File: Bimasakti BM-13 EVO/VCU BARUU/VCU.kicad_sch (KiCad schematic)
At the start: 3 parts, among them U1 Teensy4.1, U2 SN65HVD230

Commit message: add footprint library to project
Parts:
- U1: footprint (none) -> teensy4.1:Teensy41
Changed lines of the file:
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@@
 			)
 		)
-		(property "Footprint" ""
+		(property "Footprint" "teensy4.1:Teensy41"
 			(at 100.33 101.6 0)
 			(effects

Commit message: test
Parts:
- added R2: R, Resistor_SMD:R_0201_0603Metric, symbol Device:R
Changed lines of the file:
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@@
+	)
+	(symbol
+		(lib_id "Device:R")
+		(at 199.39 99.06 0)
+		(unit 1)
+		(exclude_from_sim no)
+		(in_bom yes)
+		(on_board yes)
+		(dnp no)
+		(fields_autoplaced yes)
+		(property "Reference" "R2"
+			(at 201.93 97.7899 0)
+			(effects
+				(font
+					(size 1.27 1.27)
+				)
+				(justify left)
+			)
+		)
+		(property "Value" "R"
+			(at 201.93 100.3299 0)
+			(effects
+				(font
+					(size 1.27 1.27)
+				)
+				(justify left)
+			)
+		)
+		(property "Footprint" "Resistor_SMD:R_0201_0603Metric"
+			(at 197.612 99.06 90)
+			(effects
+				(font
+					(size 1.27 1.27)
+				)
+				(hide yes)
+			)
+		)
+		(property "Datasheet" "~"
+			(at 199.39 99.06 0)
+			(effects
+				(font
+					(size 1.27 1.27)
+				)
+				(hide yes)
+			)
+		)
+		(property "Description" "Resistor"
+			(at 199.39 99.06 0)
+			(effects
+				(font
+					(size 1.27 1.27)
+				)
+				(hide yes)
+			)
+		)
+		(pin "2"
+		)
+		(pin "1"
+		)
+		(instances
+			(project ""
+				(path "/94e77d80-6817-4c0b-8f3e-96c98b3294f0"
+					(reference "R2")
+					(unit 1)
+				)
+			)
+		)
 	)
 	(symbol

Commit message: test kapasitor
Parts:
- added C1, C2, C3, C4, C5: C, symbol Device:C
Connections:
- net at R2.1: now also C3.1
- net at R2.2: now also C1.2
- new net: C4.1, C5.1
- new net: C2.1, C4.2
- new net: C1.1, C2.2

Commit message: Revert "add footprint library to project"
This reverts commit c2ea81f1652adadaa2769e08c07f448226fedb71.
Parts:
- U1: footprint teensy4.1:Teensy41 -> (none)
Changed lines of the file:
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@@
 			)
 		)
-		(property "Footprint" "teensy4.1:Teensy41"
+		(property "Footprint" ""
 			(at 100.33 101.6 0)
 			(effects

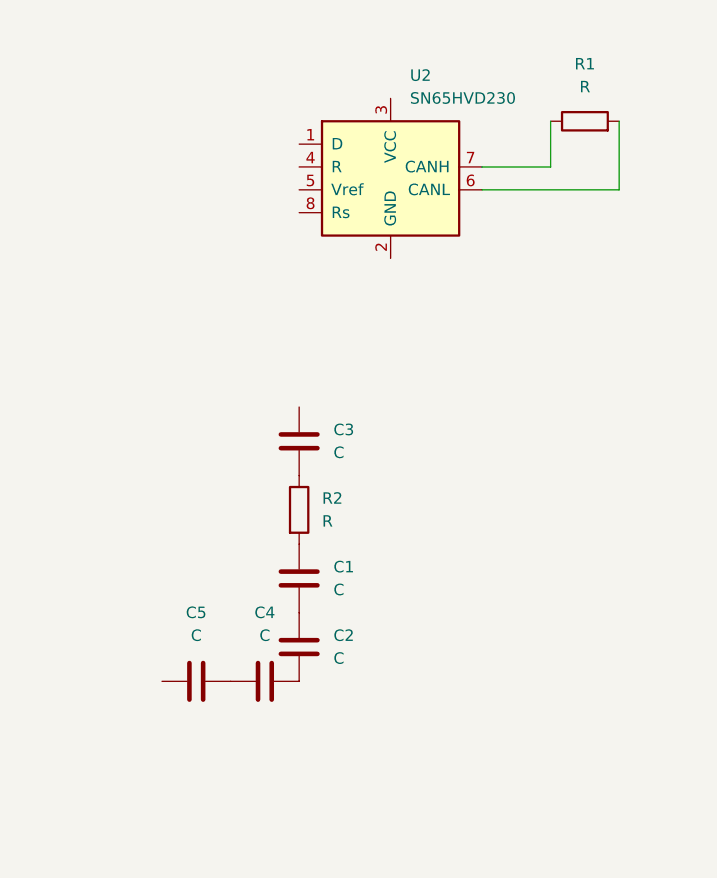
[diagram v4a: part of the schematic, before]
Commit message: Baru nambahin CAN Trans
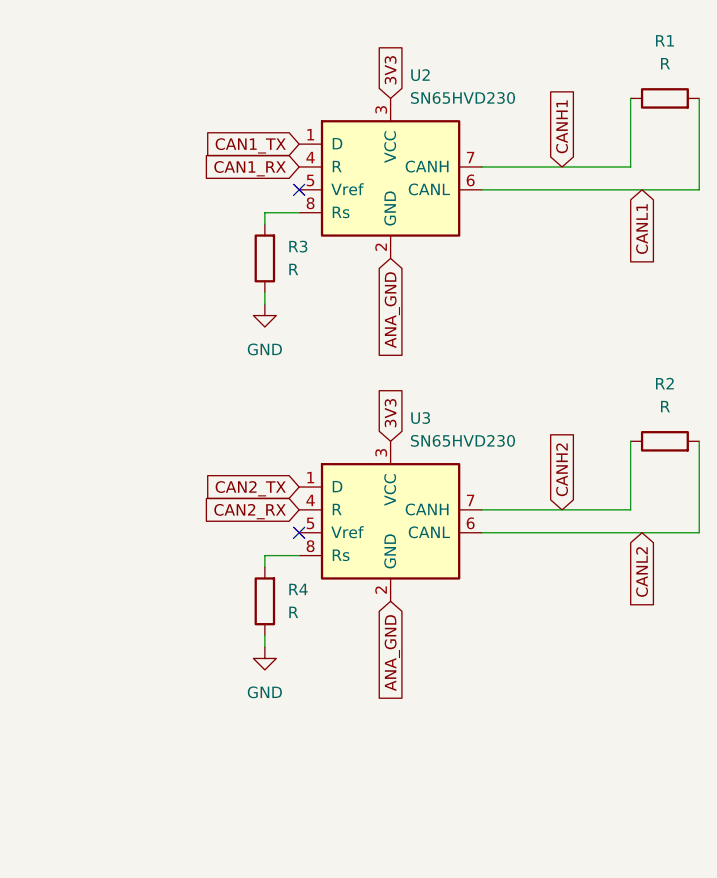
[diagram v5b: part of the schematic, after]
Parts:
- removed C1, C2, C3, C4, C5: C, symbol Device:C
- added R3, R4: R, Resistor_SMD:R_MELF_MMB-0207, symbol Device:R
- added U3: SN65HVD230, Package_SO:SOIC-8_3.9x4.9mm_P1.27mm, symbol Interface_CAN_LIN:SN65HVD230
- R2: footprint Resistor_SMD:R_0201_0603Metric -> Resistor_SMD:R_MELF_MMB-0207
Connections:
- net CANH2: now reaches R2.1
- net CANH2: now also U3.7 (CANH)
- net CANL2: now reaches R2.2
- net CANL2: now also U3.6 (CANL)
- net CANH1: now reaches R1.1, U2.7 (CANH)
- net CANL1: now reaches R1.2, U2.6 (CANL)
- net CAN1_TX: now reaches U2.1 (D)
- net ANA_GND: now reaches U2.2 (GND)
- net ANA_GND: now also U3.2 (GND)
- net 3V3: now reaches U2.3 (VCC)
- net 3V3: now also U3.3 (VCC)
- net CAN1_RX: now reaches U2.4 (R)
- net at U2.8 (Rs): now also R3.2
- new net: R4.2, U3.8 (Rs)
- new net CAN2_RX: U3.4 (R)
- new net CAN2_TX: U3.1 (D)
- new net GND: R3.1, R4.1
- no-connect marks 0 -> 2
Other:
- moved on the sheet: R1

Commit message: VCU : Nambah Can, ADS, dan Mosfet -Kertya
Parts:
- added C1: 0.1uF, Capacitor_SMD:C_0603_1608Metric, symbol Device:C
- added Q1, Q2, Q3: IRLZ44N, Package_TO_SOT_THT:TO-220-3_Vertical, symbol Transistor_FET:IRLZ44N
- added R10, R11, R9: 1K, Resistor_SMD:R_0805_2012Metric, symbol Device:R
- added R5, R6: 10K, Resistor_SMD:R_0805_2012Metric, symbol Device:R
- added R7, R8: R, Resistor_SMD:R_0805_2012Metric, symbol Device:R
- added U4: ADS1115IDGS, Package_SO:TSSOP-10_3x3mm_P0.5mm, symbol Analog_ADC:ADS1115IDGS
- added U5: SN65HVD230, Package_SO:SOIC-8_3.9x4.9mm_P1.27mm, symbol Interface_CAN_LIN:SN65HVD230
- R1, R2, R3, R4: footprint Resistor_SMD:R_MELF_MMB-0207 -> Resistor_SMD:R_0805_2012Metric
- U1: footprint (none) -> Teensy:Teensy41
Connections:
- net 3V3: now also C1.2, R5.1, R6.1, U4.8 (VDD), U5.3 (VCC)
- net ANA_GND: now also C1.1, U4.1 (ADDR), U4.3 (GND), U5.2 (GND)
- net GND: now also U1.47 (GND), Q1.3 (S), Q2.3 (S), Q3.3 (S), R10.2, R11.2, R7.1, R9.2
- net VIN: now reaches U1.48 (VIN)
- new net: R7.2, U5.8 (Rs)
- new net BAT_FAN: Q1.2 (D)
- new net BRAKE_LIGHT: Q3.2 (D)
- new net CAN3_RX: U5.4 (R)
- new net CAN3_TX: U5.1 (D)
- new net CANH3: R8.1, U5.7 (CANH)
- new net CANL3: R8.2, U5.6 (CANL)
- new net D1: Q1.1 (G), R11.1
- new net D2: Q2.1 (G), R10.1
- new net D3: Q3.1 (G), R9.1
- new net SCL: R5.2, U4.10 (SCL)
- new net SDA: R6.2, U4.9 (SDA)
- new net SWITCH_AIR: Q2.2 (D)
- no-connect marks 2 -> 68
